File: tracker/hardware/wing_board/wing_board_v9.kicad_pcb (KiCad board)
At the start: 2 copper layers, 184 x 25 mm, 12 parts, among them J1 WingTab_v9_4pin

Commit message: fix(courtyards): give the wing board real courtyard coverage + a reusable gate
The wing board advertised "0 courtyard overlap violations", which was VACUOUS:
12/12 footprints carried no F.CrtYd/B.CrtYd geometry at all, so the DRC
overlap check had nothing to compare against. The hub board (39/39) was
genuinely clean; the wing was not evidence of anything.

Added:
  * tracker/hardware/courtyard_coverage.py — generic coverage+overlap gate for
    any KiCad 9 .kicad_pcb. Reports per-footprint courtyard presence, shape,
    pad extents and the margin by which the courtyard encloses the pads, then
    computes exact pairwise intersections (rect/rect, rect/circle, circle/circle).
    Non-zero exit unless coverage is 100% AND overlaps are 0.
  * tracker/hardware/tools/courtyard_pcbnew_bbox.py — pcbnew ground-truth
    bbox harness used to validate the parser above.
  * build_wing_v9.py — emits courtyard geometry for all 12 footprints.

Result on wing_board_v9.kicad_pcb:
  coverage : 12/12 (100%)   <- was 0/12
  overlaps : 10             <- newly VISIBLE, previously unmeasurable
  verdict  : FAIL

The 10 overlaps are real and small (0.1-0.3 mm): SC1/SC2/SC3 courtyards clip
each other and the mounting holes / fiducials / RF provision pad. Now that
coverage exists they can be measured; resolving them requires a placement
nudge, which is deliberately NOT done here (no silent coordinate edits).

This commit converts a vacuous claim into a real measurement. The board is
still NOT clearance-clean.
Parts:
- removed the FID1 at (30.0, 1.70)
- removed the FID2 at (105.0, 1.70)
- removed the J1 at (0.00, 0.00)
- added FB1: FerriteBead_0402_DNP_V2only, WingV9:FerriteBead_0402_V2provision, F.Cu at (58.0, 1.70)
- added FID3: Fiducial_1mm_Mask2mm, WingV9:Fiducial_1mm_Mask2mm, F.Cu at (145.0, 1.70)
- added H1: MountingHole_NPTH_2.2mm, WingV9:MountingHole_2.2mm_NPTH, F.Cu at (8.00, 1.70)
- FID2: renamed from FB1; value FerriteBead_0402_DNP_V2only -> Fiducial_1mm_Mask2mm; footprint WingV9:FerriteBead_0402_V2provision -> WingV9:Fiducial_1mm_Mask2mm
- J1: renamed from H1; value MountingHole_NPTH_2.2mm -> WingTab_v9_4pin; footprint WingV9:MountingHole_2.2mm_NPTH -> WingV9:WingTab_v9_4pin
- moved FID1 115.0 mm to (30.0, 1.70)
- moved FID2 47.0 mm to (105.0, 1.70)
- moved J1 8.18 mm to (0.00, 0.00)
- renumbered FID3 to FID1
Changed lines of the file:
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@@
     (pad "1" smd rect (at -28 0) (size 1.6 4) (layers "F.Cu" "F.Paste" "F.Mask") (net 1 "SOLAR_P"))
     (pad "2" smd rect (at 28 0) (size 1.6 4) (layers "F.Cu" "F.Paste" "F.Mask") (net 3 "SOLAR_MID1"))
+    (fp_rect (start -29.05 -9.75) (end 29.05 9.75)
+     (stroke (width 0.05) (type solid)) (fill no) (layer "F.CrtYd"))
   )
   (footprint "WingV9:SolarCell_52x19mm"
@@
     (pad "1" smd rect (at -28 0) (size 1.6 4) (layers "F.Cu" "F.Paste" "F.Mask") (net 3 "SOLAR_MID1"))
     (pad "2" smd rect (at 28 0) (size 1.6 4) (layers "F.Cu" "F.Paste" "F.Mask") (net 4 "SOLAR_MID2"))
+    (fp_rect (start -29.05 -9.75) (end 29.05 9.75)
+     (stroke (width 0.05) (type solid)) (fill no) (layer "F.CrtYd"))
   )
   (footprint "WingV9:SolarCell_52x19mm"
@@
     (pad "1" smd rect (at -28 0) (size 1.6 4) (layers "F.Cu" "F.Paste" "F.Mask") (net 4 "SOLAR_MID2"))
     (pad "2" smd rect (at 28 0) (size 1.6 4) (layers "F.Cu" "F.Paste" "F.Mask") (net 2 "SOLAR_N"))
+    (fp_rect (start -29.05 -9.75) (end 29.05 9.75)
+     (stroke (width 0.05) (type solid)) (fill no) (layer "F.CrtYd"))
   )
   (footprint "WingV9:WingTab_v9_4pin"
@@
     (fp_text user "N" (at -5 16.9) (layer "F.SilkS") (effects (font (size 0.6 0.6) (thickness 0.1))))
     (fp_rect (start -7 8.4) (end -3 16.6) (stroke (width 0.1) (type solid)) (fill none) (layer "F.SilkS"))
+    (fp_rect (start -7.25 8.95) (end -2.75 16.05)
+     (stroke (width 0.05) (type solid)) (fill no) (layer "F.CrtYd"))
   )
   (footprint "WingV9:MountingHole_2.2mm_NPTH"
@@
     )
     (pad "" np_thru_hole circle (at 0 0) (size 2.2 2.2) (drill 2.2) (layers "*.Cu" "*.Mask"))
+    (fp_circle (center 0 0) (end 1.35 0)
+     (stroke (width 0.05) (type solid)) (fill no) (layer "F.CrtYd"))
   )
   (footprint "WingV9:MountingHole_2.2mm_NPTH"
@@
     )
     (pad "" np_thru_hole circle (at 0 0) (size 2.2 2.2) (drill 2.2) (layers "*.Cu" "*.Mask"))
+    (fp_circle (center 0 0) (end 1.35 0)
+     (stroke (width 0.05) (type solid)) (fill no) (layer "F.CrtYd"))
   )
   (footprint "WingV9:MountingHole_2.2mm_NPTH"
@@
     )
     (pad "" np_thru_hole circle (at 0 0) (size 2.2 2.2) (drill 2.2) (layers "*.Cu" "*.Mask"))
+    (fp_circle (center 0 0) (end 1.35 0)
+     (stroke (width 0.05) (type solid)) (fill no) (layer "F.CrtYd"))
   )
   (footprint "WingV9:Fiducial_1mm_Mask2mm"
@@
     (attr smd)
     (pad "1" smd circle (at 0 0) (size 1 1) (layers "F.Cu" "F.Mask"))
+    (fp_circle (center 0 0) (end 1.25 0)
+     (stroke (width 0.05) (type solid)) (fill no) (layer "F.CrtYd"))
   )
   (footprint "WingV9:Fiducial_1mm_Mask2mm"
@@
     (attr smd)
     (pad "1" smd circle (at 0 0) (size 1 1) (layers "F.Cu" "F.Mask"))
+    (fp_circle (center 0 0) (end 1.25 0)
+     (stroke (width 0.05) (type solid)) (fill no) (layer "F.CrtYd"))
   )
   (footprint "WingV9:Fiducial_1mm_Mask2mm"
@@
     (attr smd)
     (pad "1" smd circle (at 0 0) (size 1 1) (layers "F.Cu" "F.Mask"))
+    (fp_circle (center 0 0) (end 1.25 0)
+     (stroke (width 0.05) (type solid)) (fill no) (layer "F.CrtYd"))
   )
   (footprint "WingV9:FerriteBead_0402_V2provision"
@@
     (pad "1" smd rect (at -0.45 0) (size 0.5 0.6) (layers "F.Cu" "F.Paste" "F.Mask"))
     (pad "2" smd rect (at 0.45 0) (size 0.5 0.6) (layers "F.Cu" "F.Paste" "F.Mask"))
+    (fp_rect (start -0.95 -0.55) (end 0.95 0.55)
+     (stroke (width 0.05) (type solid)) (fill no) (layer "F.CrtYd"))
   )
   (footprint "WingV9:RF_ProvisionPad_v2only"
@@
     (attr smd)
     (pad "1" smd rect (at 0 0) (size 2 2) (layers "F.Cu" "F.Mask"))
+    (fp_rect (start -1.25 -1.25) (end 1.25 1.25)
+     (stroke (width 0.05) (type solid)) (fill no) (layer "F.CrtYd"))
   )
   (segment (start 2 12.5) (end 2 9.8)

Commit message: feat(wing): ADR-065 double-sided solar cells (#45)
* feat(hw/wing): parametric 3D models for the v9 wing — the 3 cells now render

The v9 wing board carried no 3D model on ANY of its 12 placed references, so a
render showed a bare FR4 outline: the three solar cells the wing exists to fly
were invisible. The hub board's models are worse than absent -- they point at
${KICAD9_3DMODEL_DIR}/...step, i.e. at kicad-packages3d (4.77 GB, NOT installed
here and not installable: ~2.3 GB free).

Added, all plain text and committed, so a render resolves with nothing installed:
  * scripts/gen_3d_models_wing.py  -- parametric VRML generator, `--check` mode
    fails closed on a stale tree. Its docstring carries the MEASURED KiCad model
    convention: 1 VRML unit = 2.54 mm, X = footprint +x, Y = -(footprint +y),
    Z = up with Z=0 at the board top face. Measured twice (a throwaway probe board
    round-tripped through `kicad-cli pcb export vrml --units mm`, plus the shipped
    ecc83.wrl demo model: 8.86 units = 22.5 mm envelope vs a 21.2 mm courtyard).
  * tracker/hardware/3dmodels/cells/  -- the SMALL cell 52.07 x 19.65 x 0.21
    (ADR-049 measured inputs; the board's own footprint is SolarCell_52x19mm) as
    the wing's cell model, plus the LARGE 78.55 x 38.90 x 0.21 as a SHARED,
    unassigned asset for the hub/array direction. cells/ is named for sharing so
    the parallel hub worker reuses them instead of duplicating.
  * tracker/hardware/3dmodels/wing/   -- J1's four 4.0x1.2 lands at 1.8 mm pitch,
    the FID1-3 1 mm dots, the FB1 0402 body (DNP -> rendered translucent so it
    cannot be mistaken for a fitted part), and RF1's V2 provision land.
  * build_wing_v9.py + the regenerated board: +99 lines / 0 deletions, all of it
    (model ...) metadata. Proven unchanged by parsing both revisions and
    set-comparing nets (17), footprints (12 with lib id / ref / position / every
    pad), segments (8), Edge.Cuts (8), gr_text (1) and thickness. No net, no part
    position a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
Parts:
- added SC4: SolarCell_52x19mm_0.5V, WingV9:SolarCell_52x19mm, B.Cu at (30.0, 12.5)
- added SC5: SolarCell_52x19mm_0.5V, WingV9:SolarCell_52x19mm, B.Cu at (88.0, 12.5)
- added SC6: SolarCell_52x19mm_0.5V, WingV9:SolarCell_52x19mm, B.Cu at (146.0, 12.5)

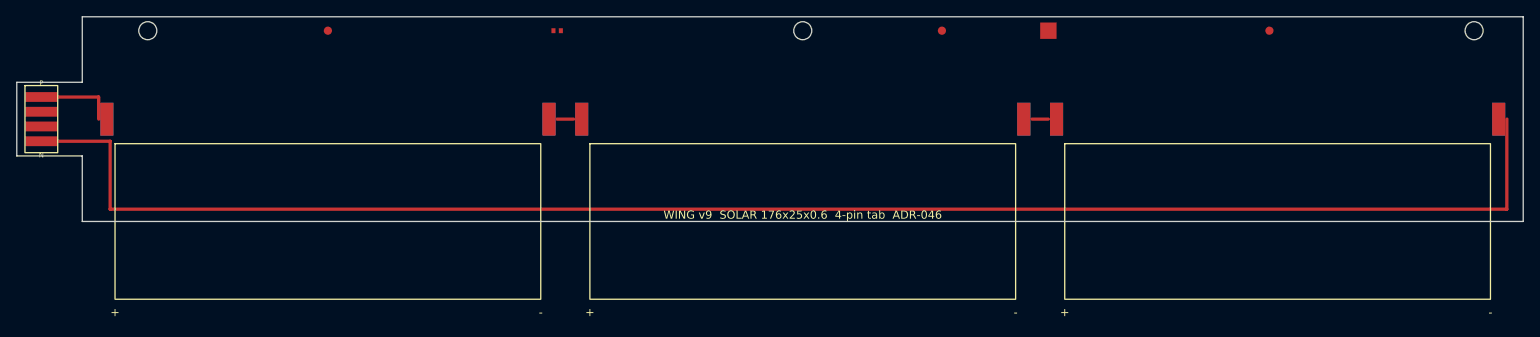
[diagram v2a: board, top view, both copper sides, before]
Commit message: fix(wing): wire the B.Cu solar back string (ADR-065 shipped placement only)
build_wing_v9.py emitted segments on F.Cu only, so on a 2-layer board whose
cells now sat on B.Cu the back series string was electrically isolated: zero
B.Cu tracks, zero vias, 12 unconnected items.

The real defect was worse than "no segments". cell_footprint laid the back-face
cells out with X-mirrored pad geometry but front-face net order, making the back
series chain a bowtie: SOLAR_MID1 would have to jump x=3 -> x=115 mm across two
cells, and every via attempt shorted SOLAR_MID1 into SOLAR_MID2 because the F.Cu
and B.Cu tracks sat at different gaps.

Fix: the back cell is the same cell tipped over its LONG axis (180 deg about X,
terminals keep their X), so back pads sit directly beneath the front pads on the
same net and the back landing coordinates are identical to the front. The back
string is drawn pad-centre to pad-centre with through vias tying each node's
F.Cu and B.Cu halves together (tangential land contact is not a KiCad
connection).

kicad-cli pcb drc (KiCad 9.0.8), same board before vs after:
  unconnected_items 12 -> 0
  track_dangling     4 -> 2
  every other class unchanged

Result: 20 segments (F.Cu + B.Cu) and 2 vias, monotonic back chain. pcbnew
confirms SC4/SC5/SC6 are SMD lands on B.Cu, exactly co-axial with SC1/SC2/SC3
above them, on the same nets.

Docs: ADR-065 addendum (the interconnect gap and the bowtie root cause).
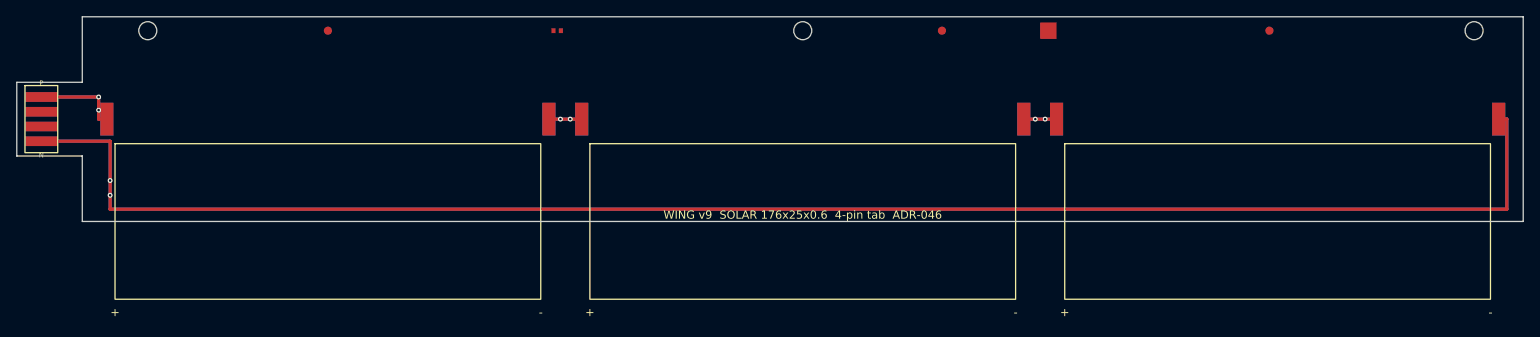
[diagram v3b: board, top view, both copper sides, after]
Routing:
- net SOLAR_N: track 198.3 -> 398.6 mm, vias 0 -> 2
- net SOLAR_P: track 9.70 -> 21.4 mm, vias 0 -> 2
- net SOLAR_MID2: track 2.00 -> 8.00 mm, vias 0 -> 2
- net SOLAR_MID1: track 2.00 -> 8.00 mm, vias 0 -> 2
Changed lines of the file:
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@@
     (attr smd)
     (fp_rect (start -26 3) (end 26 22) (stroke (width 0.12) (type solid)) (fill no) (layer "B.SilkS"))
-    (fp_text user "+" (at 26 23.6) (layer "B.SilkS") (effects (font (size 1 1) (thickness 0.12))))
-    (fp_text user "-" (at -26 23.6) (layer "B.SilkS") (effects (font (size 1 1) (thickness 0.12))))
-    (pad "1" smd rect (at 27 0) (size 1.6 4) (layers "B.Cu" "B.Paste" "B.Mask") (net 1 "SOLAR_P"))
-    (pad "2" smd rect (at -27 0) (size 1.6 4) (layers "B.Cu" "B.Paste" "B.Mask") (net 3 "SOLAR_MID1"))
+    (fp_text user "+" (at -26 23.6) (layer "B.SilkS") (effects (font (size 1 1) (thickness 0.12))))
+    (fp_text user "-" (at 26 23.6) (layer "B.SilkS") (effects (font (size 1 1) (thickness 0.12))))
+    (pad "1" smd rect (at -27 0) (size 1.6 4) (layers "B.Cu" "B.Paste" "B.Mask") (net 1 "SOLAR_P"))
+    (pad "2" smd rect (at 27 0) (size 1.6 4) (layers "B.Cu" "B.Paste" "B.Mask") (net 3 "SOLAR_MID1"))
     (fp_rect (start -28.05 -2.25) (end 28.05 2.25) (stroke (width 0.05) (type solid)) (fill no) (layer "B.CrtYd"))
     (model "${KIPRJMOD}/../3dmodels/cells/solar_cell_small_52.07x19.65x0.21.wrl"
@@
     (attr smd)
     (fp_rect (start -26 3) (end 26 22) (stroke (width 0.12) (type solid)) (fill no) (layer "B.SilkS"))
-    (fp_text user "+" (at 26 23.6) (layer "B.SilkS") (effects (font (size 1 1) (thickness 0.12))))
-    (fp_text user "-" (at -26 23.6) (layer "B.SilkS") (effects (font (size 1 1) (thickness 0.12))))
-    (pad "1" smd rect (at 27 0) (size 1.6 4) (layers "B.Cu" "B.Paste" "B.Mask") (net 3 "SOLAR_MID1"))
-    (pad "2" smd rect (at -27 0) (size 1.6 4) (layers "B.Cu" "B.Paste" "B.Mask") (net 4 "SOLAR_MID2"))
+    (fp_text user "+" (at -26 23.6) (layer "B.SilkS") (effects (font (size 1 1) (thickness 0.12))))
+    (fp_text user "-" (at 26 23.6) (layer "B.SilkS") (effects (font (size 1 1) (thickness 0.12))))
+    (pad "1" smd rect (at -27 0) (size 1.6 4) (layers "B.Cu" "B.Paste" "B.Mask") (net 3 "SOLAR_MID1"))
+    (pad "2" smd rect (at 27 0) (size 1.6 4) (layers "B.Cu" "B.Paste" "B.Mask") (net 4 "SOLAR_MID2"))
     (fp_rect (start -28.05 -2.25) (end 28.05 2.25) (stroke (width 0.05) (type solid)) (fill no) (layer "B.CrtYd"))
     (model "${KIPRJMOD}/../3dmodels/cells/solar_cell_small_52.07x19.65x0.21.wrl"
@@
     (attr smd)
     (fp_rect (start -26 3) (end 26 22) (stroke (width 0.12) (type solid)) (fill no) (layer "B.SilkS"))
-    (fp_text user "+" (at 26 23.6) (layer "B.SilkS") (effects (font (size 1 1) (thickness 0.12))))
-    (fp_text user "-" (at -26 23.6) (layer "B.SilkS") (effects (font (size 1 1) (thickness 0.12))))
-    (pad "1" smd rect (at 27 0) (size 1.6 4) (layers "B.Cu" "B.Paste" "B.Mask") (net 4 "SOLAR_MID2"))
-    (pad "2" smd rect (at -27 0) (size 1.6 4) (layers "B.Cu" "B.Paste" "B.Mask") (net 2 "SOLAR_N"))
+    (fp_text user "+" (at -26 23.6) (layer "B.SilkS") (effects (font (size 1 1) (thickness 0.12))))
+    (fp_text user "-" (at 26 23.6) (layer "B.SilkS") (effects (font (size 1 1) (thickness 0.12))))
+    (pad "1" smd rect (at -27 0) (size 1.6 4) (layers "B.Cu" "B.Paste" "B.Mask") (net 4 "SOLAR_MID2"))
+    (pad "2" smd rect (at 27 0) (size 1.6 4) (layers "B.Cu" "B.Paste" "B.Mask") (net 2 "SOLAR_N"))
     (fp_rect (start -28.05 -2.25) (end 28.05 2.25) (stroke (width 0.05) (type solid)) (fill no) (layer "B.CrtYd"))
     (model "${KIPRJMOD}/../3dmodels/cells/solar_cell_small_52.07x19.65x0.21.wrl"
@@
     )
   )
+  (segment (start 3 12.5) (end 2 12.5)
+    (width 0.4) (layer "F.Cu") (net 1))
   (segment (start 2 12.5) (end 2 9.8)
     (width 0.4) (layer "F.Cu") (net 1))
   (segment (start 2 9.8) (end -5 9.8)
     (width 0.4) (layer "F.Cu") (net 1))
-  (segment (start 58 12.5) (end 60 12.5)
+  (segment (start 57 12.5) (end 61 12.5)
     (width 0.4) (layer "F.Cu") (net 3))
-  (segment (start 116 12.5) (end 118 12.5)
+  (segment (start 115 12.5) (end 119 12.5)
     (width 0.4) (layer "F.Cu") (net 4))
+  (segment (start 173 12.5) (end 174 12.5)
+    (width 0.4) (layer "F.Cu") (net 2))
   (segment (start 174 12.5) (end 174 23.5)
     (width 0.4) (layer "F.Cu") (net 2))
@@
   (segment (start 3.4 15.2) (end -5 15.2)
     (width 0.4) (layer "F.Cu") (net 2))
+  (segment (start 3 12.5) (end 2 12.5)
+    (width 0.4) (layer "B.Cu") (net 1))
+  (segment (start 2 12.5) (end 2 9.8)
+    (width 0.4) (layer "B.Cu") (net 1))
+  (segment (start 2 9.8) (end -5 9.8)
+    (width 0.4) (layer "B.Cu") (net 1))
+  (segment (start 57 12.5) (end 61 12.5)
+    (width 0.4) (layer "B.Cu") (net 3))
+  (segment (start 115 12.5) (end 119 12.5)
+    (width 0.4) (layer "B.Cu") (net 4))
+  (segment (start 173 12.5) (end 174 12.5)
+    (width 0.4) (layer "B.Cu") (net 2))
+  (segment (start 174 12.5) (end 174 23.5)
+    (width 0.4) (layer "B.Cu") (net 2))
+  (segment (start 174 23.5) (end 3.4 23.5)
+    (width 0.4) (layer "B.Cu") (net 2))
+  (segment (start 3.4 23.5) (end 3.4 15.2)
+    (width 0.4) (layer "B.Cu") (net 2))
+  (segment (start 3.4 15.2) (end -5 15.2)
+    (width 0.4) (layer "B.Cu") (net 2))
+  (via (at 2 9.8) (size 0.6) (drill 0.3)
+    (layers "F.Cu" "B.Cu") (net 1))
+  (via (at 2 11.4) (size 0.6) (drill 0.3)
+    (layers "F.Cu" "B.Cu") (net 1))
+  (via (at 58.4 12.5) (size 0.6) (drill 0.3)
+    (layers "F.Cu" "B.Cu") (net 3))
+  (via (at 59.6 12.5) (size 0.6) (drill 0.3)
+    (layers "F.Cu" "B.Cu") (net 3))
+  (via (at 116.4 12.5) (size 0.6) (drill 0.3)
+    (layers "F.Cu" "B.Cu") (net 4))
+  (via (at 117.6 12.5) (size 0.6) (drill 0.3)
+    (layers "F.Cu" "B.Cu") (net 4))
+  (via (at 3.4 20) (size 0.6) (drill 0.3)
+    (layers "F.Cu" "B.Cu") (net 2))
+  (via (at 3.4 21.8) (size 0.6) (drill 0.3)
+    (layers "F.Cu" "B.Cu") (net 2))
   (gr_text "WING v9  SOLAR 176x25x0.6  4-pin tab  ADR-046" (at 88 24.2 0) (layer "F.SilkS")
     (effects (font (size 1.0 1.0) (thickness 0.12))))
